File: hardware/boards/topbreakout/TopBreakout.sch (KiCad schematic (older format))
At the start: 0 parts

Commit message: minor
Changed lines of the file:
@@
 S 1000 1000 500  150
 U 5D7F4208
-F0 "io_breakout-ver2.1_1" 50
+F0 "D/A jack connectors" 50
 F1 "io_breakout-ver2.1_1.sch" 50
 $EndSheet
@@
 S 3000 1000 500  150
 U 5D7F4281
-F0 "io_breakout-ver2.1_2" 50
+F0 "A D Connectors" 50
 F1 "io_breakout-ver2.1_2.sch" 50
 $EndSheet
@@
 S 5000 1000 500  150
 U 5D7F42FA
-F0 "io_breakout-ver2.1_3" 50
+F0 "FPC connector" 50
 F1 "io_breakout-ver2.1_3.sch" 50
 $EndSheet
@@
 S 7000 1000 500  150
 U 5D7F4364
-F0 "io_breakout-ver2.1_4" 50
+F0 "TFT Connector" 50
 F1 "io_breakout-ver2.1_4.sch" 50
 $EndSheet
@@
 S 9000 1000 500  150
 U 5D7F4383
-F0 "io_breakout-ver2.1_5" 50
+F0 "AD7606" 50
 F1 "io_breakout-ver2.1_5.sch" 50
 $EndSheet
@@
 S 1000 3000 500  150
 U 5D7F4465
-F0 "io_breakout-ver2.1_6" 50
+F0 "AD5754 DAC" 50
 F1 "io_breakout-ver2.1_6.sch" 50
 $EndSheet

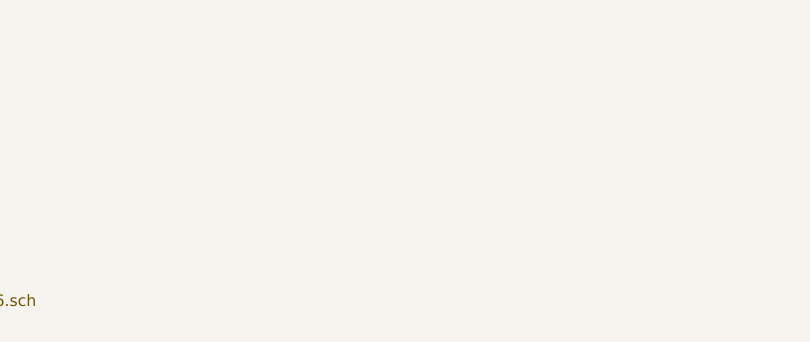
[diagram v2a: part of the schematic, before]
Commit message: moved midi circuit to breakout board
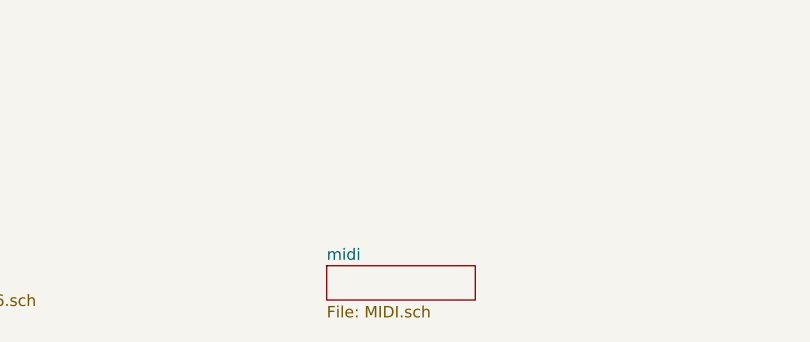
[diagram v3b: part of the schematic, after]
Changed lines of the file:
@@
 $Descr A4 11693 8268
 encoding utf-8
-Sheet 1 7
+Sheet 1 8
 Title ""
 Date ""
@@
 F1 "io_breakout-ver2.1_6.sch" 50
 $EndSheet
+$Sheet
+S 3300 3050 650  150
+U 5D8CF794
+F0 "midi" 50
+F1 "MIDI.sch" 50
+$EndSheet
 $EndSCHEMATC

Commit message: mainboard v1.7
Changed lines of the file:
@@
-EESchema Schematic File Version 5
+EESchema Schematic File Version 4
 EELAYER 30 0
 EELAYER END
@@
 Comment3 ""
 Comment4 ""
-Comment5 ""
-Comment6 ""
-Comment7 ""
-Comment8 ""
-Comment9 ""
 $EndDescr
 $Sheet
-S 1000 1000 500  150
+S 1000 5150 500  150
 U 5D7F4208
 F0 "D/A jack connectors" 50
@@
 $EndSheet
 $Sheet
-S 3000 1000 500  150
+S 3000 5150 500  150
 U 5D7F4281
 F0 "A D Connectors" 50
@@
 $EndSheet
 $Sheet
-S 5000 1000 500  150
+S 5000 5150 500  150
 U 5D7F42FA
 F0 "FPC connector" 50
@@
 $EndSheet
 $Sheet
-S 7000 1000 500  150
+S 7000 5150 500  150
 U 5D7F4364
 F0 "TFT Connector" 50
@@
 $EndSheet
 $Sheet
-S 9000 1000 500  150
+S 9000 5150 500  150
 U 5D7F4383
 F0 "AD7606" 50
@@
 $EndSheet
 $Sheet
-S 1000 3000 500  150
+S 1000 7150 500  150
 U 5D7F4465
 F0 "AD5754 DAC" 50
@@
 $EndSheet
 $Sheet
-S 3300 3050 650  150
+S 3300 7200 650  150
 U 5D8CF794
 F0 "midi" 50
